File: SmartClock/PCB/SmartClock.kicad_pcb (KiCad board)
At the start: 2 copper layers, 53 x 30 mm, 3 parts, among them SW1 SW_Push, U2 XIAO-ESP32-C3-DIP

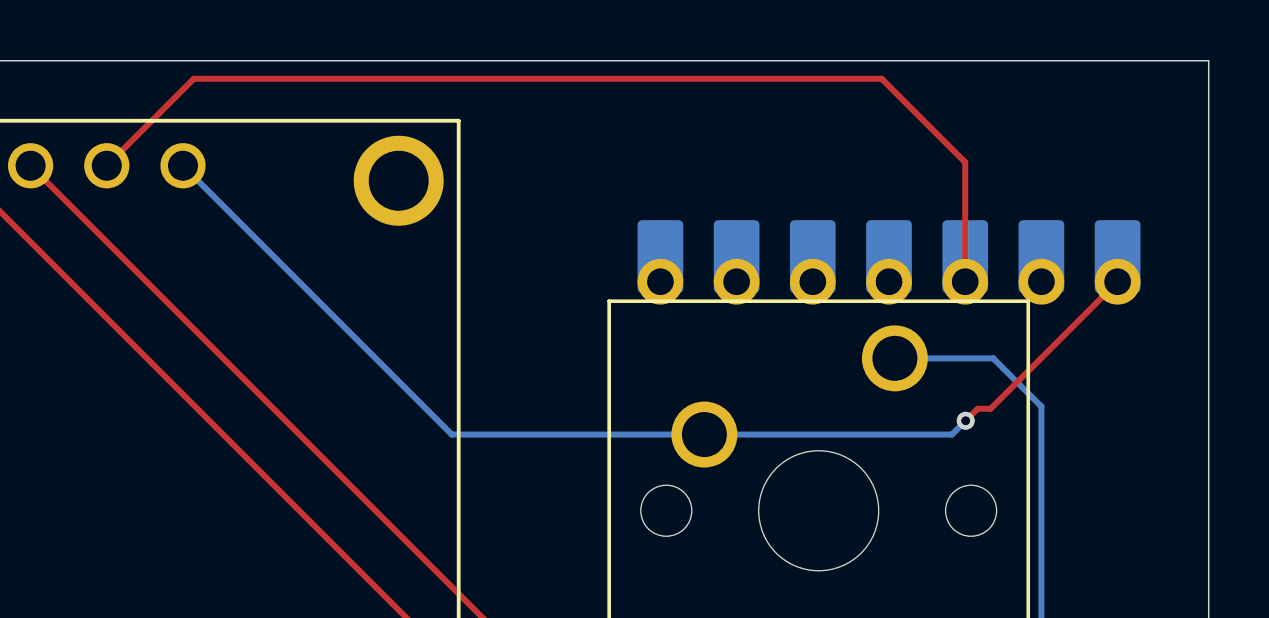
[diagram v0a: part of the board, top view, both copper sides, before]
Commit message: pcb Fix + Gerber
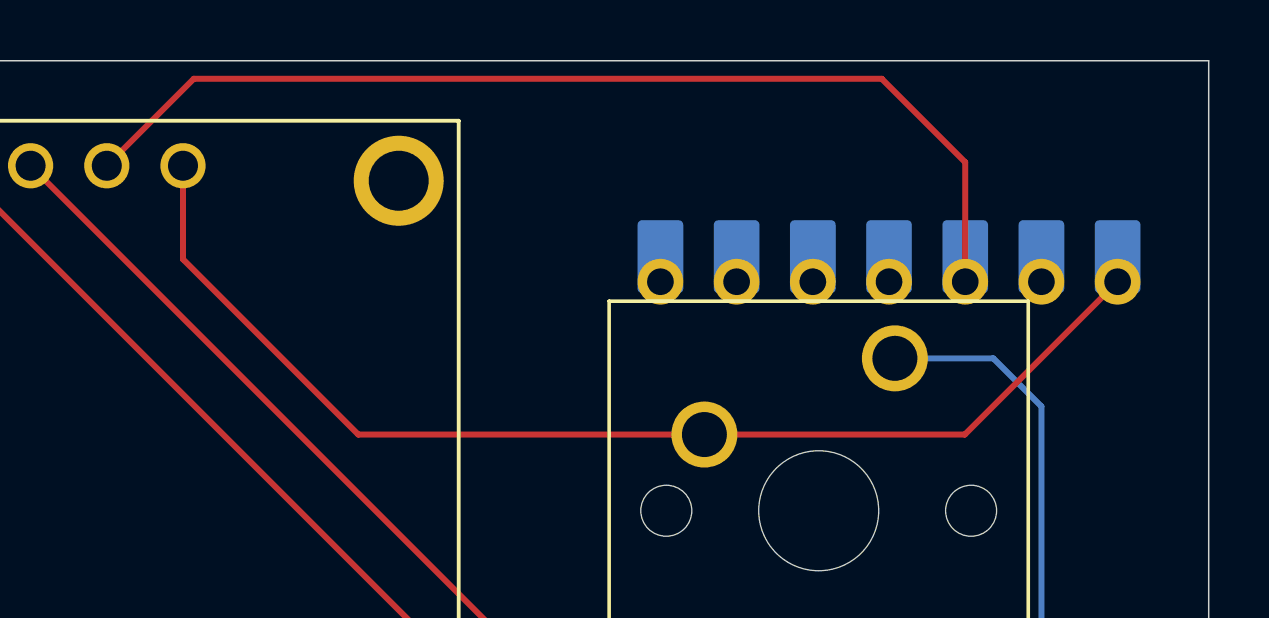
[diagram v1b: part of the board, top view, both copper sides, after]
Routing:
- net GND: track 37.0 -> 38.8 mm, vias 1 -> 0
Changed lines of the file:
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@@
 			(outputformat 1)
 			(mirror no)
-			(drillshape 1)
+			(drillshape 0)
 			(scaleselection 1)
-			(outputdirectory "")
+			(outputdirectory "./")
 		)
 	)
@@
 	)
 	(segment
-		(start 150.8 45.6)
-		(end 151.229723 45.6)
+		(start 141.69 46.46)
+		(end 150.369723 46.46)
 		(width 0.2)
 		(layer "F.Cu")
@@
 	)
 	(segment
-		(start 151.229723 45.6)
+		(start 130.153 46.46)
+		(end 141.69 46.46)
+		(width 0.2)
+		(layer "F.Cu")
+		(net 13)
+	)
+	(segment
+		(start 124.31 37.5)
+		(end 124.31 40.617)
+		(width 0.2)
+		(layer "F.Cu")
+		(net 13)
+	)
+	(segment
+		(start 150.369723 46.46)
 		(end 155.463962 41.365761)
 		(width 0.2)
@@
 	)
 	(segment
-		(start 150.4 46)
-		(end 150.8 45.6)
+		(start 124.31 40.617)
+		(end 130.153 46.46)
 		(width 0.2)
 		(layer "F.Cu")
 		(net 13)
 	)
-	(via
-		(at 150.4 46)
-		(size 0.6)
-		(drill 0.3)
-		(layers "F.Cu" "B.Cu")
-		(net 13)
-	)
-	(segment
-		(start 133.27 46.46)
-		(end 141.69 46.46)
-		(width 0.2)
-		(layer "B.Cu")
-		(net 13)
-	)
-	(segment
-		(start 149.94 46.46)
-		(end 150.4 46)
-		(width 0.2)
-		(layer "B.Cu")
-		(net 13)
-	)
-	(segment
-		(start 124.31 37.5)
-		(end 133.27 46.46)
-		(width 0.2)
-		(layer "B.Cu")
-		(net 13)
-	)
-	(segment
-		(start 141.69 46.46)
-		(end 149.94 46.46)
-		(width 0.2)
-		(layer "B.Cu")
-		(net 13)
-	)
